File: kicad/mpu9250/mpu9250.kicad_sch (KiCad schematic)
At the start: 37 parts, among them J1 USB4125-GF-A_REVA, J2 Conn_02x03_Odd_Even, J3 Conn_01x05, J4 Conn_01x02, SW1 SW_SPDT, U1 MCP73832-2-OT, U2 BQ297xy, U3 CSD85302L, U4 NCP177BMX330TCG, U5 BMI160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

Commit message: stated work on mpu9250 not finnished
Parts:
- removed C6, C7: 100nf, Capacitor_SMD:C_0402_1005Metric, symbol Device:C
- removed U5: BMI160, Package_LGA:Bosch_LGA-14_3x2.5mm_P0.5mm, symbol Sensor_Motion:BMI160
- added C? (x3): 100nf, symbol Device:C
- added U?: mpu9250, symbol mpu9250:mpu9250
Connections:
- net MOSI is gone; now on net ADDRESS: J3.5 (Pin_5)
- net +3.3V: now also C?.2, C?.2, U?.1 (RESV), U?.13 (VDD), U?.22 (nCS), U?.8 (VDDIO)
- net ADDRESS: now also U?.9 (AD0/SD0)
- net GND: now also C?.1, C?.1, C?.1, U?.11 (FSYNC), U?.18 (GND), U?.20 (RESV)
- net H_SCL: now also U?.23 (SCL/SCLK)
- net H_SDA: now also U?.24 (SDA/SDI)
- new net: C?.2, U?.10 (REGOUT)
- new net: U?.14 (NC), U?.15 (NC), U?.16 (NC), U?.17 (NC), U?.19 (RESV), U?.2 (NC), U?.3 (NC), U?.4 (NC), U?.5 (NC), U?.6 (NC)
- no-connect marks 14 -> 11
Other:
- note added: "MPU9250"
- note removed: "BMI160"
- moved on the sheet: JP1, R15, R16

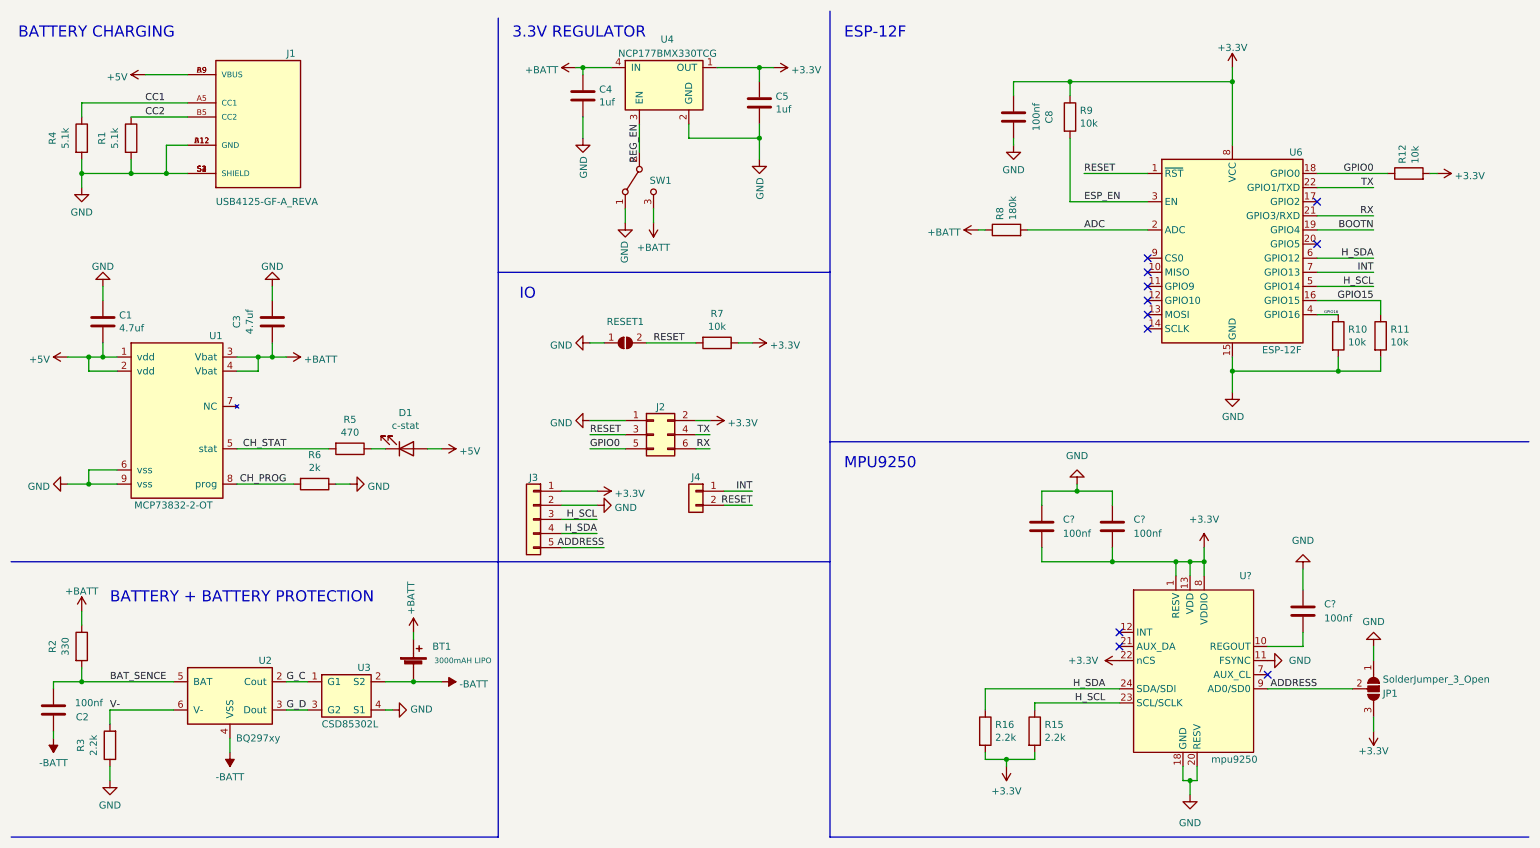
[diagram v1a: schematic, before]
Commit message: added support for mpu9250
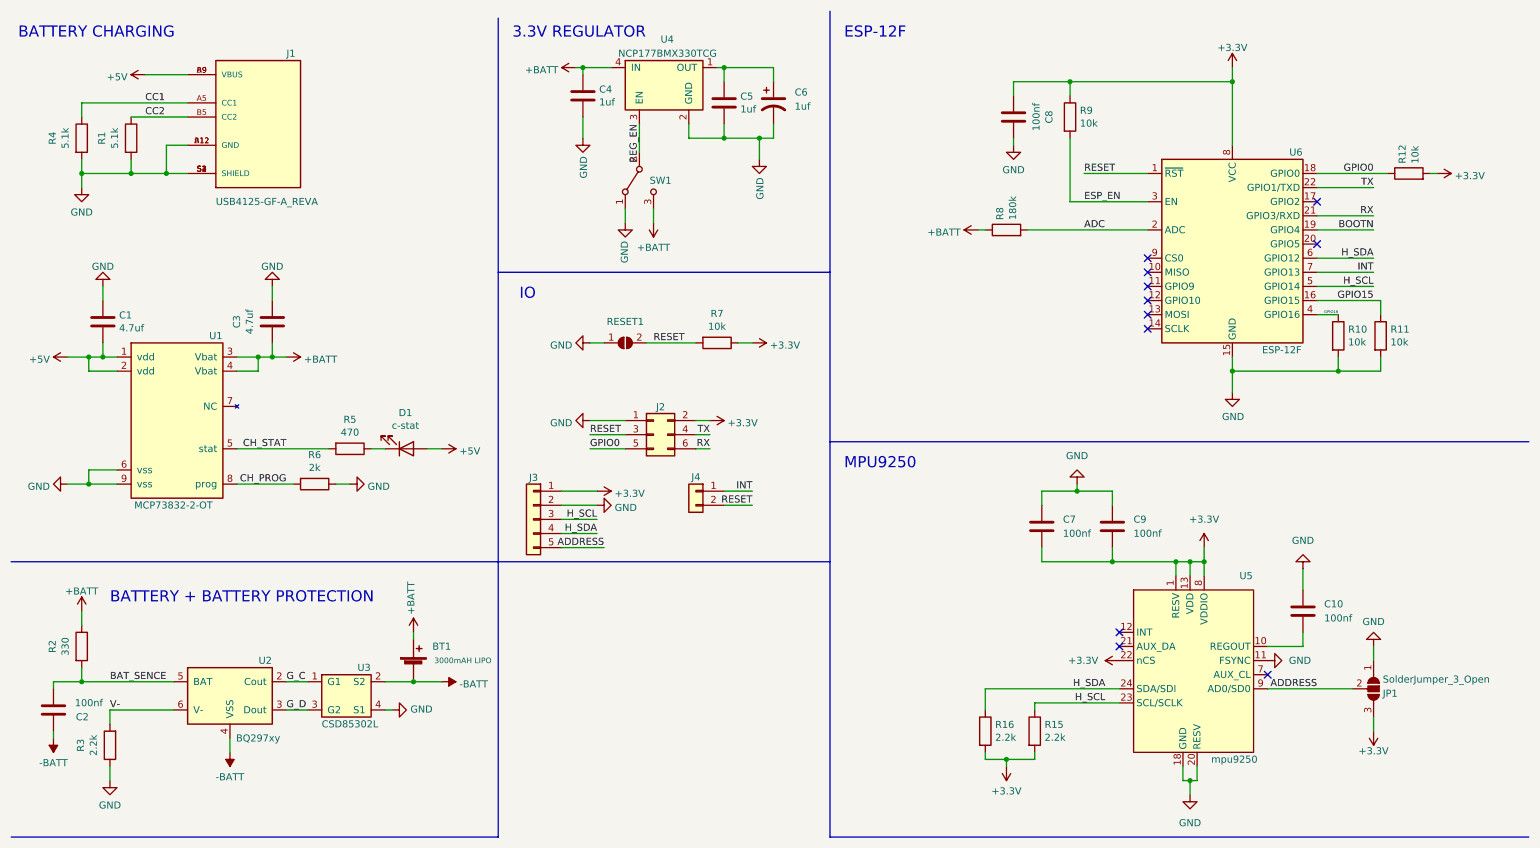
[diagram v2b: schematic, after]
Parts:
- added C6: 1uf, Capacitor_SMD:CP_Elec_4x4.5, symbol Device:C_Polarized_US
- C10, C7, C9: renamed from C?; footprint (none) -> Capacitor_SMD:C_0402_1005Metric
- U5: renamed from U?; footprint (none) -> Package_DFN_QFN:QFN-24-1EP_3x3mm_P0.4mm_EP1.75x1.6mm
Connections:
- net +3.3V: no longer C5.1, U4.1 (OUT)
- net GND: now also C6.2
- new net: C5.1, C6.1, U4.1 (OUT)
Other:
- moved on the sheet: C5
